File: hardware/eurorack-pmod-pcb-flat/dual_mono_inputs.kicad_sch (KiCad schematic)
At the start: 15 parts, among them J5 PJ398SM, J6 PJ398SM, U4 TL074, U5 TL074

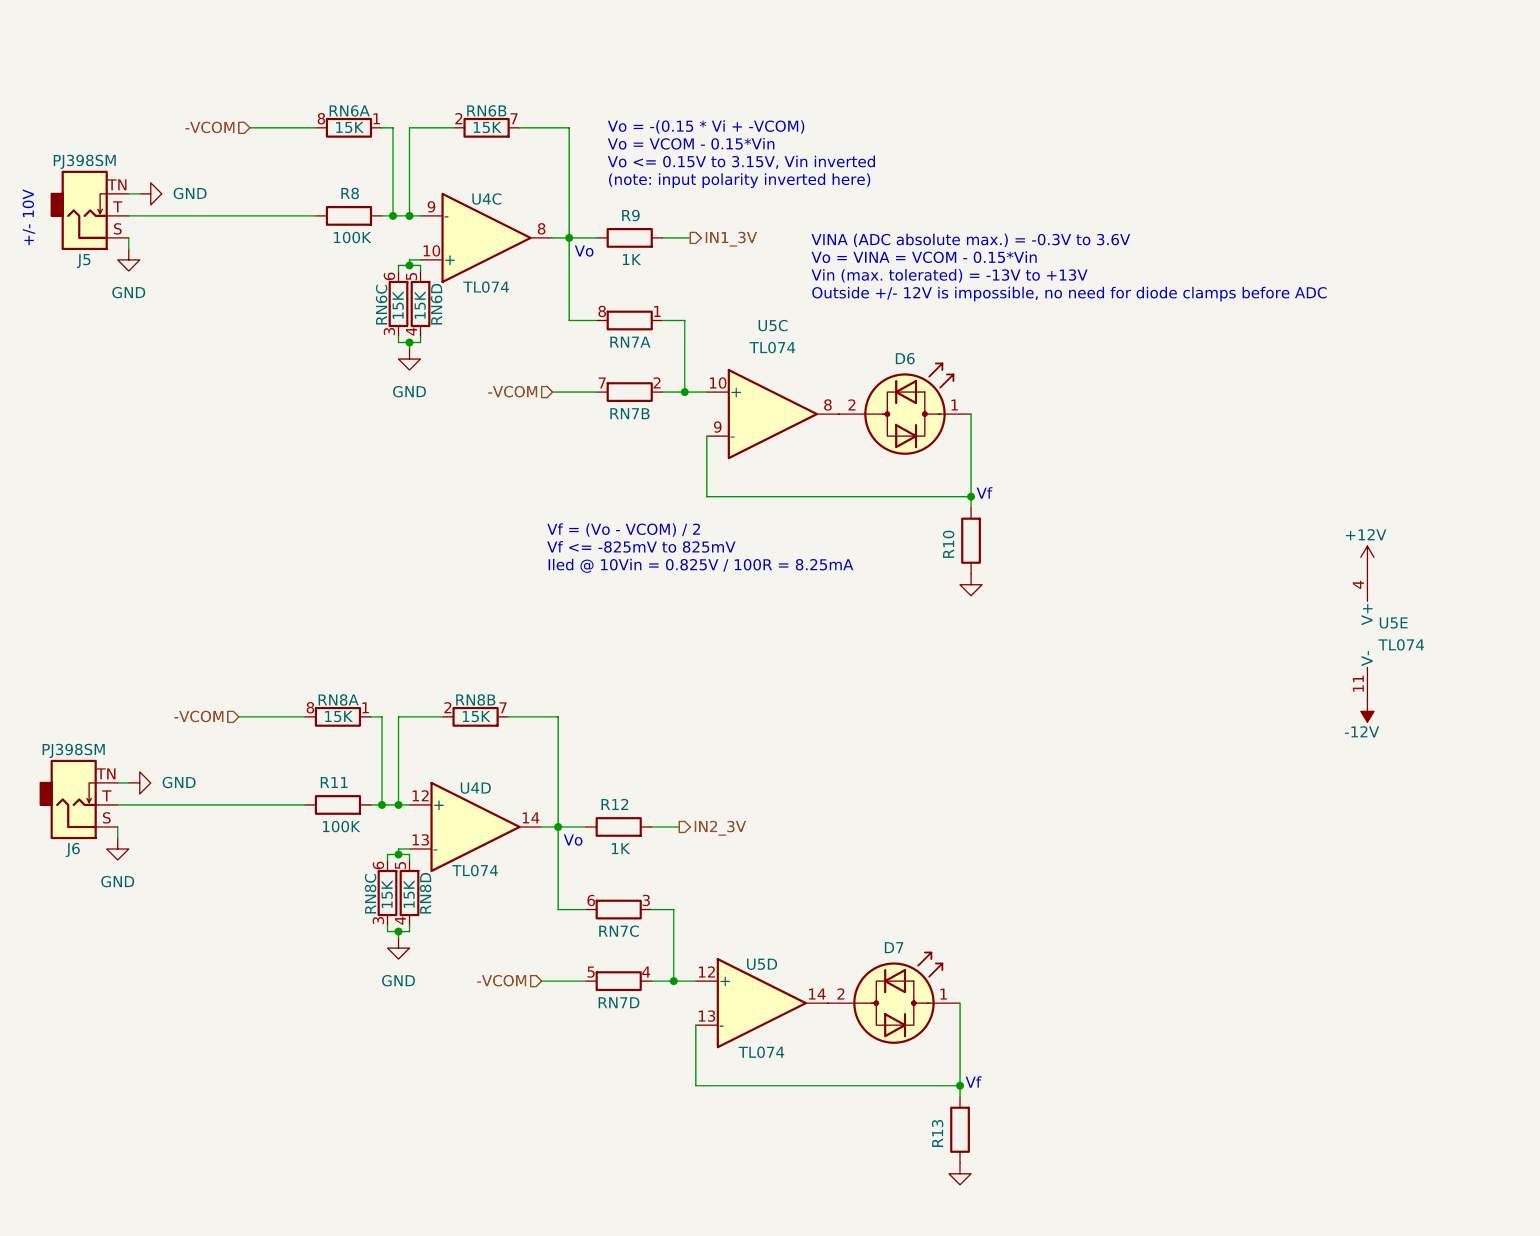
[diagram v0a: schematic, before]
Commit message: rev2-flat: add vref and stabilization caps
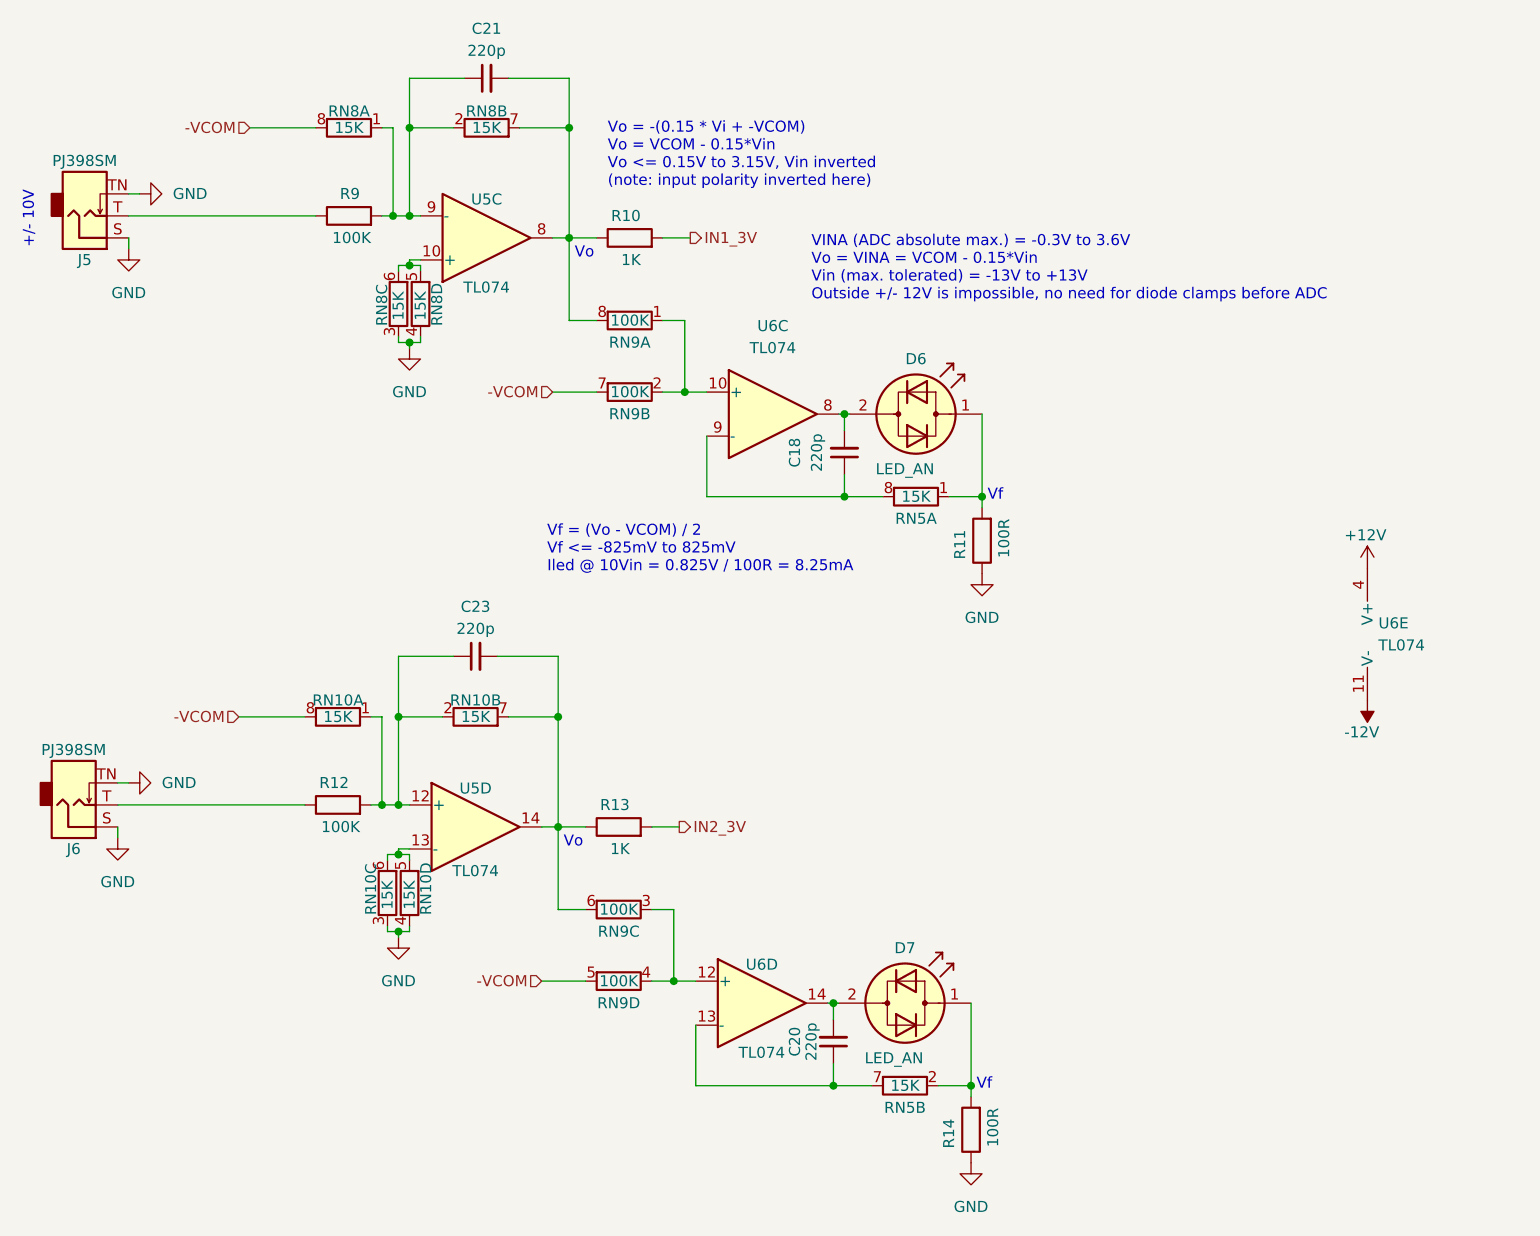
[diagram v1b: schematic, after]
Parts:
- added C18, C20, C21, C23: 220p, Capacitor_SMD:C_0603_1608Metric, symbol Device:C_Small
- added RN5: 15K, Resistor_SMD:R_Cat16-4, symbol Device:R_Pack04_Split
- D6, D7: value (none) -> LED_AN
- R11: renamed from R10; value (none) -> 100R
- R14: renamed from R13; value (none) -> 100R
- RN9: renamed from RN7; value (none) -> 100K
- renumbered R9 to R10, R11 to R12, R12 to R13, R8 to R9, RN8 to RN10, RN6 to RN8, U4 to U5, U5 to U6
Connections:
- net at R12.2, RN10.1 (R1.1), RN10.2 (R2.1)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: now also C23.1
- net at R13.1, RN10.7 (R2.2), RN9.6 (R3.2)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: now also C23.2
- net at R10.1, RN8.7 (R2.2), RN9.8 (R1.2)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: now also C21.2
- net at R9.2, RN8.1 (R1.1), RN8.2 (R2.1)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: now also C21.1
- net at D7.1 (KA), R14.2: now also RN5.2 (R2.1); no longer U6.13 (-)
- net at D7.2 (AK), U6.14: now also C20.2
- net at D6.1 (KA), R11.2: now also RN5.1 (R1.1); no longer U6.9 (-)
- net at D6.2 (AK), U6.8: now also C18.2
- new net: C18.1, RN5.8 (R1.2), U6.9 (-)
- new net: C20.1, RN5.7 (R2.2), U6.13 (-)
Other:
- moved on the sheet: D6, D7, R11, R14

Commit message: rev2-flat: update power supply and add bypass electros
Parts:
- renumbered C21 to C24, C18 to C25, C23 to C26, C20 to C27, D6 to D5, D7 to D6, R11 to R10, R12 to R11, R13 to R12, R14 to R13, R9 to R8, R10 to R9, RN8 to RN7, RN9 to RN8, RN10 to RN9, U5 to U4, U6 to U5
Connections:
- net at D5.1 (KA), R10.2: now also RN5.3 (R3.1); no longer RN5.1 (R1.1)
- net at C25.1, U5.9 (-): now also RN5.6 (R3.2); no longer RN5.8 (R1.2)
- net at C27.1, U5.13 (-): now also RN5.5 (R4.2); no longer RN5.7 (R2.2)
- net at D6.1 (KA), R13.2: now also RN5.4 (R4.1); no longer RN5.2 (R2.1)

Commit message: rev2-flat: update fields and fab1 export
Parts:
- RN5, RN7, RN9: dig# CAY16-1502F4LFCT-ND -> CAT16-1502F4LFCT-ND; mfg# CAY16-1502F4LF -> CAT16-1502F4LF
- RN8: dig# CAY16-1003F4LFCT-ND -> CAT16-1003F4LFCT-ND; mfg# CAY16-1003F4LF -> CAT16-1003F4LF
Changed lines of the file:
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@@
       (effects (font (size 1.27 1.27)) hide)
     )
-    (property "dig#" "CAY16-1502F4LFCT-ND" (id 4) (at 78.105 94.615 0)
-      (effects (font (size 1.27 1.27)) hide)
-    )
-    (property "mfg#" "CAY16-1502F4LF" (id 5) (at 78.105 94.615 0)
+    (property "dig#" "CAT16-1502F4LFCT-ND" (id 4) (at 78.105 94.615 0)
+      (effects (font (size 1.27 1.27)) hide)
+    )
+    (property "mfg#" "CAT16-1502F4LF" (id 5) (at 78.105 94.615 0)
       (effects (font (size 1.27 1.27)) hide)
     )
@@
       (effects (font (size 1.27 1.27)) hide)
     )
-    (property "dig#" "CAY16-1502F4LFCT-ND" (id 4) (at 128.905 69.215 0)
-      (effects (font (size 1.27 1.27)) hide)
-    )
-    (property "mfg#" "CAY16-1502F4LF" (id 5) (at 128.905 69.215 0)
+    (property "dig#" "CAT16-1502F4LFCT-ND" (id 4) (at 128.905 69.215 0)
+      (effects (font (size 1.27 1.27)) hide)
+    )
+    (property "mfg#" "CAT16-1502F4LF" (id 5) (at 128.905 69.215 0)
       (effects (font (size 1.27 1.27)) hide)
     )
@@
       (effects (font (size 1.27 1.27)) hide)
     )
-    (property "dig#" "CAY16-1003F4LFCT-ND" (id 4) (at 94.615 125.095 0)
-      (effects (font (size 1.27 1.27)) hide)
-    )
-    (property "mfg#" "CAY16-1003F4LF" (id 5) (at 94.615 125.095 0)
+    (property "dig#" "CAT16-1003F4LFCT-ND" (id 4) (at 94.615 125.095 0)
+      (effects (font (size 1.27 1.27)) hide)
+    )
+    (property "mfg#" "CAT16-1003F4LF" (id 5) (at 94.615 125.095 0)
       (effects (font (size 1.27 1.27)) hide)
     )
@@
       (effects (font (size 1.27 1.27)) hide)
     )
-    (property "dig#" "CAY16-1502F4LFCT-ND" (id 4) (at 127.635 137.16 0)
-      (effects (font (size 1.27 1.27)) hide)
-    )
-    (property "mfg#" "CAY16-1502F4LF" (id 5) (at 127.635 137.16 0)
+    (property "dig#" "CAT16-1502F4LFCT-ND" (id 4) (at 127.635 137.16 0)
+      (effects (font (size 1.27 1.27)) hide)
+    )
+    (property "mfg#" "CAT16-1502F4LF" (id 5) (at 127.635 137.16 0)
       (effects (font (size 1.27 1.27)) hide)
     )
@@
       (effects (font (size 1.27 1.27)) hide)
     )
-    (property "dig#" "CAY16-1502F4LFCT-ND" (id 4) (at 69.215 46.99 0)
-      (effects (font (size 1.27 1.27)) hide)
-    )
-    (property "mfg#" "CAY16-1502F4LF" (id 5) (at 69.215 46.99 0)
+    (property "dig#" "CAT16-1502F4LFCT-ND" (id 4) (at 69.215 46.99 0)
+      (effects (font (size 1.27 1.27)) hide)
+    )
+    (property "mfg#" "CAT16-1502F4LF" (id 5) (at 69.215 46.99 0)
       (effects (font (size 1.27 1.27)) hide)
     )
@@
       (effects (font (size 1.27 1.27)) hide)
     )
-    (property "dig#" "CAY16-1502F4LFCT-ND" (id 4) (at 63.5 26.67 0)
-      (effects (font (size 1.27 1.27)) hide)
-    )
-    (property "mfg#" "CAY16-1502F4LF" (id 5) (at 63.5 26.67 0)
+    (property "dig#" "CAT16-1502F4LFCT-ND" (id 4) (at 63.5 26.67 0)
+      (effects (font (size 1.27 1.27)) hide)
+    )
+    (property "mfg#" "CAT16-1502F4LF" (id 5) (at 63.5 26.67 0)
       (effects (font (size 1.27 1.27)) hide)
     )
@@
       (effects (font (size 1.27 1.27)) hide)
     )
-    (property "dig#" "CAY16-1003F4LFCT-ND" (id 4) (at 95.885 48.895 0)
-      (effects (font (size 1.27 1.27)) hide)
-    )
-    (property "mfg#" "CAY16-1003F4LF" (id 5) (at 95.885 48.895 0)
+    (property "dig#" "CAT16-1003F4LFCT-ND" (id 4) (at 95.885 48.895 0)
+      (effects (font (size 1.27 1.27)) hide)
+    )
+    (property "mfg#" "CAT16-1003F4LF" (id 5) (at 95.885 48.895 0)
       (effects (font (size 1.27 1.27)) hide)
     )
@@
       (effects (font (size 1.27 1.27)) hide)
     )
-    (property "dig#" "CAY16-1003F4LFCT-ND" (id 4) (at 95.885 57.15 0)
-      (effects (font (size 1.27 1.27)) hide)
-    )
-    (property "mfg#" "CAY16-1003F4LF" (id 5) (at 95.885 57.15 0)
+    (property "dig#" "CAT16-1003F4LFCT-ND" (id 4) (at 95.885 57.15 0)
+      (effects (font (size 1.27 1.27)) hide)
+    )
+    (property "mfg#" "CAT16-1003F4LF" (id 5) (at 95.885 57.15 0)
       (effects (font (size 1.27 1.27)) hide)
     )
@@
       (effects (font (size 1.27 1.27)) hide)
     )
-    (property "dig#" "CAY16-1502F4LFCT-ND" (id 4) (at 70.485 114.935 0)
-      (effects (font (size 1.27 1.27)) hide)
-    )
-    (property "mfg#" "CAY16-1502F4LF" (id 5) (at 70.485 114.935 0)
+    (property "dig#" "CAT16-1502F4LFCT-ND" (id 4) (at 70.485 114.935 0)
+      (effects (font (size 1.27 1.27)) hide)
+    )
+    (property "mfg#" "CAT16-1502F4LF" (id 5) (at 70.485 114.935 0)
       (effects (font (size 1.27 1.27)) hide)
     )
@@
       (effects (font (size 1.27 1.27)) hide)
     )
-    (property "dig#" "CAY16-1502F4LFCT-ND" (id 4) (at 62.23 94.615 0)
-      (effects (font (size 1.27 1.27)) hide)
-    )
-    (property "mfg#" "CAY16-1502F4LF" (id 5) (at 62.23 94.615 0)
+    (property "dig#" "CAT16-1502F4LFCT-ND" (id 4) (at 62.23 94.615 0)
+      (effects (font (size 1.27 1.27)) hide)
+    )
+    (property "mfg#" "CAT16-1502F4LF" (id 5) (at 62.23 94.615 0)
       (effects (font (size 1.27 1.27)) hide)
     )
@@
       (effects (font (size 1.27 1.27)) hide)
     )
-    (property "dig#" "CAY16-1502F4LFCT-ND" (id 4) (at 67.945 114.935 0)
-      (effects (font (size 1.27 1.27)) hide)
-    )
-    (property "mfg#" "CAY16-1502F4LF" (id 5) (at 67.945 114.935 0)
+    (property "dig#" "CAT16-1502F4LFCT-ND" (id 4) (at 67.945 114.935 0)
+      (effects (font (size 1.27 1.27)) hide)
+    )
+    (property "mfg#" "CAT16-1502F4LF" (id 5) (at 67.945 114.935 0)
       (effects (font (size 1.27 1.27)) hide)
     )
@@
       (effects (font (size 1.27 1.27)) hide)
     )
-    (property "dig#" "CAY16-1502F4LFCT-ND" (id 4) (at 79.375 26.67 0)
-      (effects (font (size 1.27 1.27)) hide)
-    )
-    (property "mfg#" "CAY16-1502F4LF" (id 5) (at 79.375 26.67 0)
+    (property "dig#" "CAT16-1502F4LFCT-ND" (id 4) (at 79.375 26.67 0)
+      (effects (font (size 1.27 1.27)) hide)
+    )
+    (property "mfg#" "CAT16-1502F4LF" (id 5) (at 79.375 26.67 0)
       (effects (font (size 1.27 1.27)) hide)
     )
@@
       (effects (font (size 1.27 1.27)) hide)
     )
-    (property "dig#" "CAY16-1502F4LFCT-ND" (id 4) (at 71.755 46.99 0)
-      (effects (font (size 1.27 1.27)) hide)
-    )
-    (property "mfg#" "CAY16-1502F4LF" (id 5) (at 71.755 46.99 0)
+    (property "dig#" "CAT16-1502F4LFCT-ND" (id 4) (at 71.755 46.99 0)
+      (effects (font (size 1.27 1.27)) hide)
+    )
+    (property "mfg#" "CAT16-1502F4LF" (id 5) (at 71.755 46.99 0)
       (effects (font (size 1.27 1.27)) hide)
     )
@@
       (effects (font (size 1.27 1.27)) hide)
     )
-    (property "dig#" "CAY16-1003F4LFCT-ND" (id 4) (at 94.615 116.84 0)
-      (effects (font (size 1.27 1.27)) hide)
-    )
-    (property "mfg#" "CAY16-1003F4LF" (id 5) (at 94.615 116.84 0)
-      (effects (font (size 1.27 1.27)) hide)
-    )
+    (property "dig#" "CAT16-1003F4LFCT-ND" (id 4) (at 94.615 116.84 0)
+      (effects (font (size 1.27 1.27)) hide)
+    )
+    (property "mfg#" "CAT16-1003F4LF" (id 5) (at 94.615 116.84 0)
+      (effects (font (size 1.27 1.27)) hide)
+    )

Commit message: rev3: add notes, fix flipped op-amp
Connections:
- net at C26.1, R11.2, RN9.1 (R1.1)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: now also U4.13 (-); no longer U4.12 (+)
- net at RN9.5 (R4.2), RN9.6 (R3.2): now also U4.12 (+); no longer U4.13 (-)
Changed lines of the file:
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@@
     (pin "2")
   )
-  (symbol (lib_id "Amplifier_Operational:TL074") (at 78.105 107.315 0) (unit 4)
+  (symbol (lib_id "Amplifier_Operational:TL074") (at 78.105 107.315 0) (mirror x) (unit 4)
     (in_bom yes) (on_board yes)
-    (property "Reference" "U4" (id 0) (at 78.105 102.87 0))
+    (property "Reference" "U4" (id 0) (at 78.105 102.235 0))
     (property "Value" "TL074" (id 1) (at 78.105 112.395 0))
-    (property "Footprint" "Package_SO:TSSOP-14_4.4x5mm_P0.65mm" (id 2) (at 76.835 104.775 0)
+    (property "Footprint" "Package_SO:TSSOP-14_4.4x5mm_P0.65mm" (id 2) (at 76.835 109.855 0)
       (effects (font (size 1.27 1.27)) hide)
     )
-    (property "Datasheet" "http://www.ti.com/lit/ds/symlink/tl071.pdf" (id 3) (at 79.375 102.235 0)
+    (property "Datasheet" "http://www.ti.com/lit/ds/symlink/tl071.pdf" (id 3) (at 79.375 112.395 0)
       (effects (font (size 1.27 1.27)) hide)
     )
